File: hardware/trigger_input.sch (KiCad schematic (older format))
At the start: 7 parts

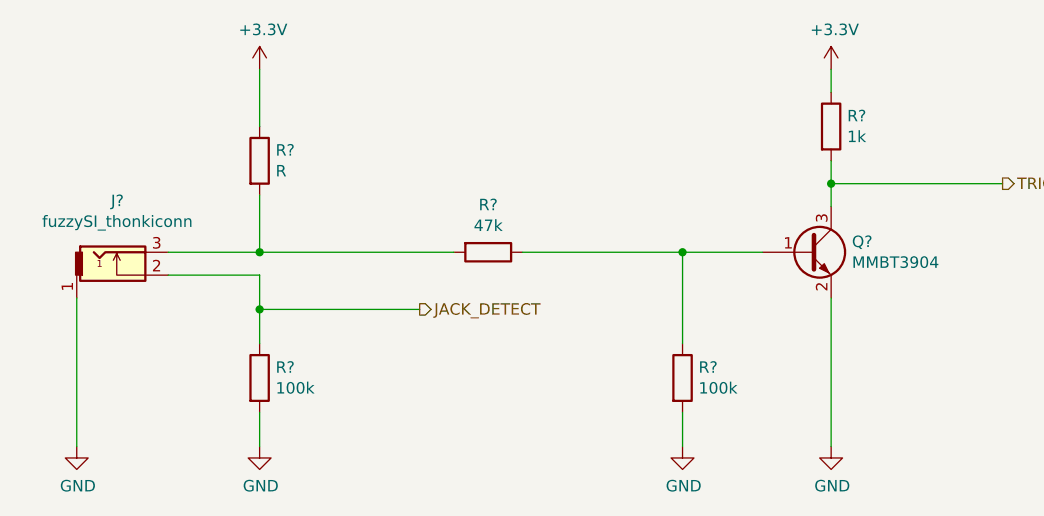
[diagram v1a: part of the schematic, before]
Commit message: Add CV-out schematics
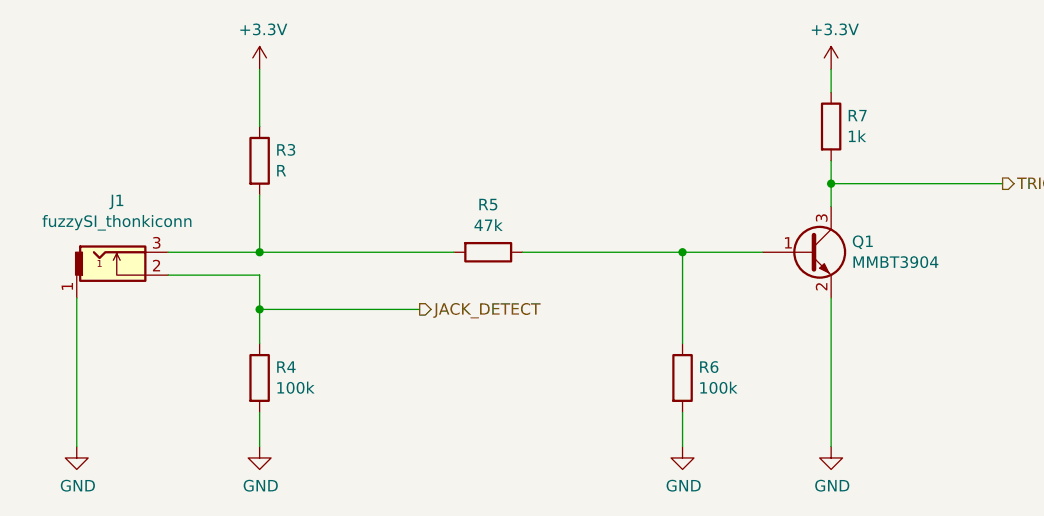
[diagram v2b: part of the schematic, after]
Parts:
- gave numbers to parts that had none: 7
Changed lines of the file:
@@
 $Descr A4 11693 8268
 encoding utf-8
-Sheet 2 3
+Sheet 2 4
 Title ""
 Date ""
@@
 $EndDescr
 $Comp
-L power:+3.3V #PWR?
+L power:+3.3V #PWR06
 U 1 1 5ED56FD6
 P 4700 2650
-F 0 "#PWR?" H 4700 2500 50  0001 C CNN
+F 0 "#PWR06" H 4700 2500 50  0001 C CNN
 F 1 "+3.3V" H 4715 2823 50  0000 C CNN
 F 2 "" H 4700 2650 50  0001 C CNN
@@
 $EndComp
 $Comp
-L power:GND #PWR?
+L power:GND #PWR07
 U 1 1 5ED578BC
 P 4700 4300
-F 0 "#PWR?" H 4700 4050 50  0001 C CNN
+F 0 "#PWR07" H 4700 4050 50  0001 C CNN
 F 1 "GND" H 4705 4127 50  0000 C CNN
 F 2 "" H 4700 4300 50  0001 C CNN
@@
 $EndComp
 $Comp
-L Transistor_BJT:MMBT3904 Q?
+L Transistor_BJT:MMBT3904 Q1
 U 1 1 5ED5AD18
 P 7100 3450
-F 0 "Q?" H 7291 3496 50  0000 L CNN
+F 0 "Q1" H 7291 3496 50  0000 L CNN
 F 1 "MMBT3904" H 7291 3405 50  0000 L CNN
 F 2 "Package_TO_SOT_SMD:SOT-23" H 7300 3375 50  0001 L CIN
@@
 $EndComp
 $Comp
-L Device:R R?
+L Device:R R3
 U 1 1 5ED61718
 P 4700 3050
-F 0 "R?" H 4770 3096 50  0000 L CNN
+F 0 "R3" H 4770 3096 50  0000 L CNN
 F 1 "R" H 4770 3005 50  0000 L CNN
 F 2 "" V 4630 3050 50  0001 C CNN
@@
 $EndComp
 $Comp
-L Device:R R?
+L Device:R R7
 U 1 1 5ED61C77
 P 7200 2900
-F 0 "R?" H 7270 2946 50  0000 L CNN
+F 0 "R7" H 7270 2946 50  0000 L CNN
 F 1 "1k" H 7270 2855 50  0000 L CNN
 F 2 "" V 7130 2900 50  0001 C CNN
@@
 $EndComp
 $Comp
-L Device:R R?
+L Device:R R4
 U 1 1 5ED61E0C
 P 4700 4000
-F 0 "R?" H 4770 4046 50  0000 L CNN
+F 0 "R4" H 4770 4046 50  0000 L CNN
 F 1 "100k" H 4770 3955 50  0000 L CNN
 F 2 "" V 4630 4000 50  0001 C CNN
@@
 $EndComp
 $Comp
-L Device:R R?
+L Device:R R5
 U 1 1 5ED62145
 P 5700 3450
-F 0 "R?" V 5493 3450 50  0000 C CNN
+F 0 "R5" V 5493 3450 50  0000 C CNN
 F 1 "47k" V 5584 3450 50  0000 C CNN
 F 2 "" V 5630 3450 50  0001 C CNN
@@
 $EndComp
 $Comp
-L Device:R R?
+L Device:R R6
 U 1 1 5ED6232E
 P 6550 4000
-F 0 "R?" H 6620 4046 50  0000 L CNN
+F 0 "R6" H 6620 4046 50  0000 L CNN
 F 1 "100k" H 6620 3955 50  0000 L CNN
 F 2 "" V 6480 4000 50  0001 C CNN
@@
 	4700 2650 4700 2900
 $Comp
-L power:+3.3V #PWR?
+L power:+3.3V #PWR09
 U 1 1 5ED6C9CF
 P 7200 2650
-F 0 "#PWR?" H 7200 2500 50  0001 C CNN
+F 0 "#PWR09" H 7200 2500 50  0001 C CNN
 F 1 "+3.3V" H 7215 2823 50  0000 C CNN
 F 2 "" H 7200 2650 50  0001 C CNN
@@
 Connection ~ 6550 3450
 $Comp
-L power:GND #PWR?
+L power:GND #PWR08
 U 1 1 5ED7253E
 P 6550 4300
-F 0 "#PWR?" H 6550 4050 50  0001 C CNN
+F 0 "#PWR08" H 6550 4050 50  0001 C CNN
 F 1 "GND" H 6555 4127 50  0000 C CNN
 F 2 "" H 6550 4300 50  0001 C CNN
@@
 	6550 4300 6550 4150
 $Comp
-L power:GND #PWR?
+L power:GND #PWR010
 U 1 1 5ED73092
 P 7200 4300
-F 0 "#PWR?" H 7200 4050 50  0001 C CNN
+F 0 "#PWR010" H 7200 4050 50  0001 C CNN
 F 1 "GND" H 7205 4127 50  0000 C CNN
 F 2 "" H 7200 4300 50  0001 C CNN
@@
 	3900 3650 3900 4300
 $Comp
-L power:GND #PWR?
+L power:GND #PWR05
 U 1 1 5ED63404
 P 3900 4300
-F 0 "#PWR?" H 3900 4050 50  0001 C CNN
+F 0 "#PWR05" H 3900 4050 50  0001 C CNN
 F 1 "GND" H 3905 4127 50  0000 C CNN
 F 2 "" H 3900 4300 50  0001 C CNN
@@
 $EndComp
 $Comp
-L thonkiconn_jackSocket_fuzzySi:fuzzySI_thonkiconn J?
+L thonkiconn_jackSocket_fuzzySi:fuzzySI_thonkiconn J1
 U 1 1 5ED5F1B0
 P 4100 3550
-F 0 "J?" H 4078 3875 50  0000 C CNN
+F 0 "J1" H 4078 3875 50  0000 C CNN
 F 1 "fuzzySI_thonkiconn" H 4078 3784 50  0000 C CNN
 F 2 "" H 4350 3650 50  0001 C CNN

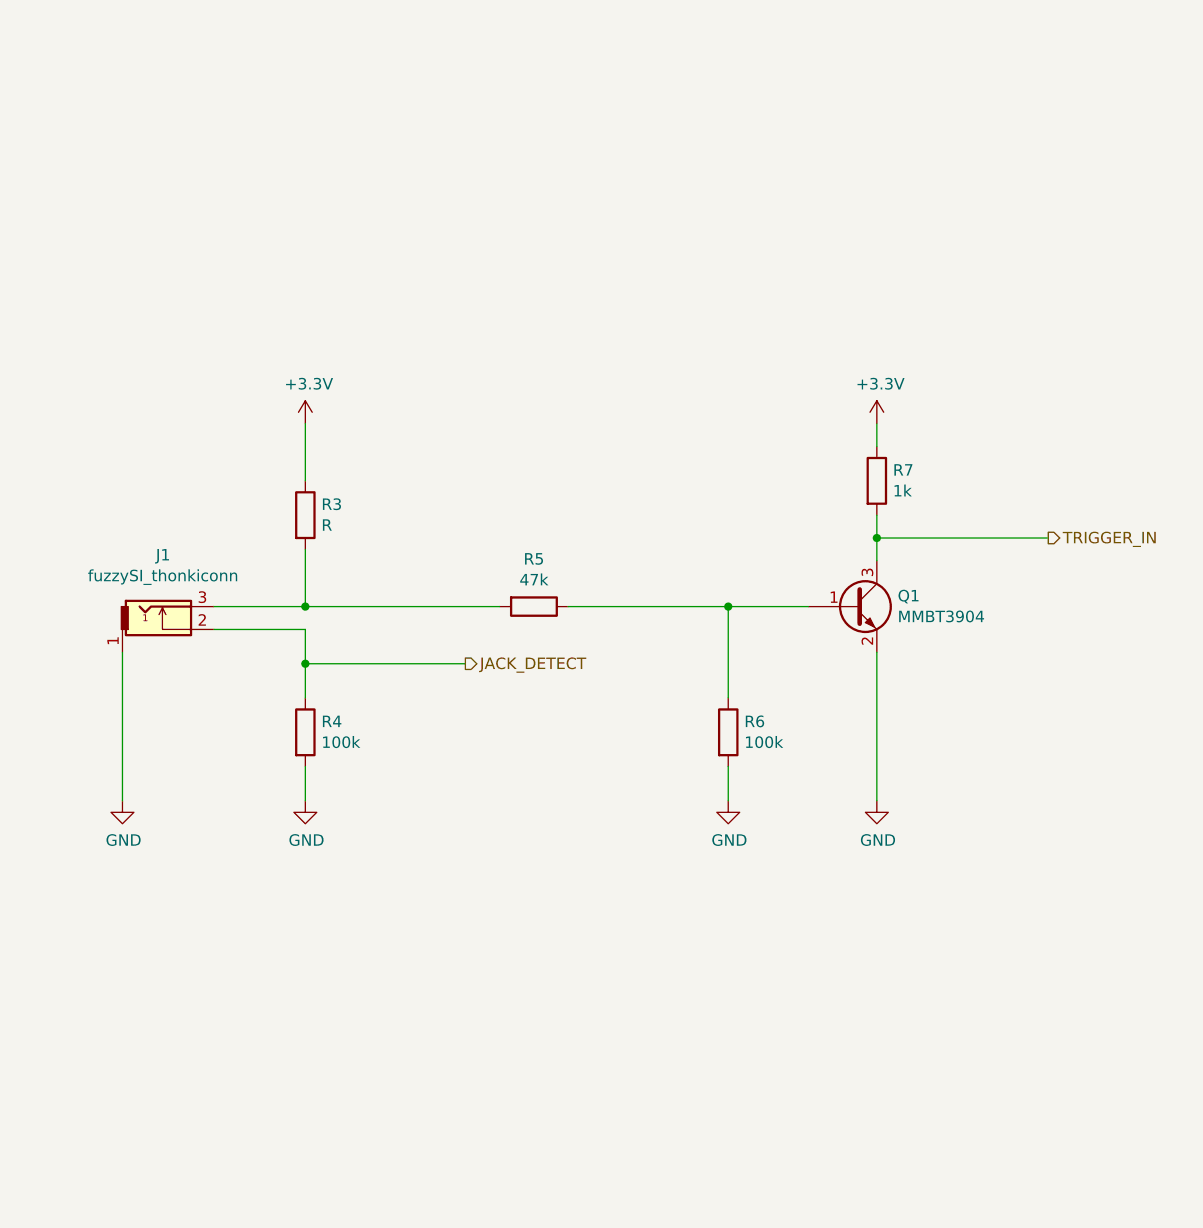
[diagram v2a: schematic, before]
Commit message: Add CV inputs schematics
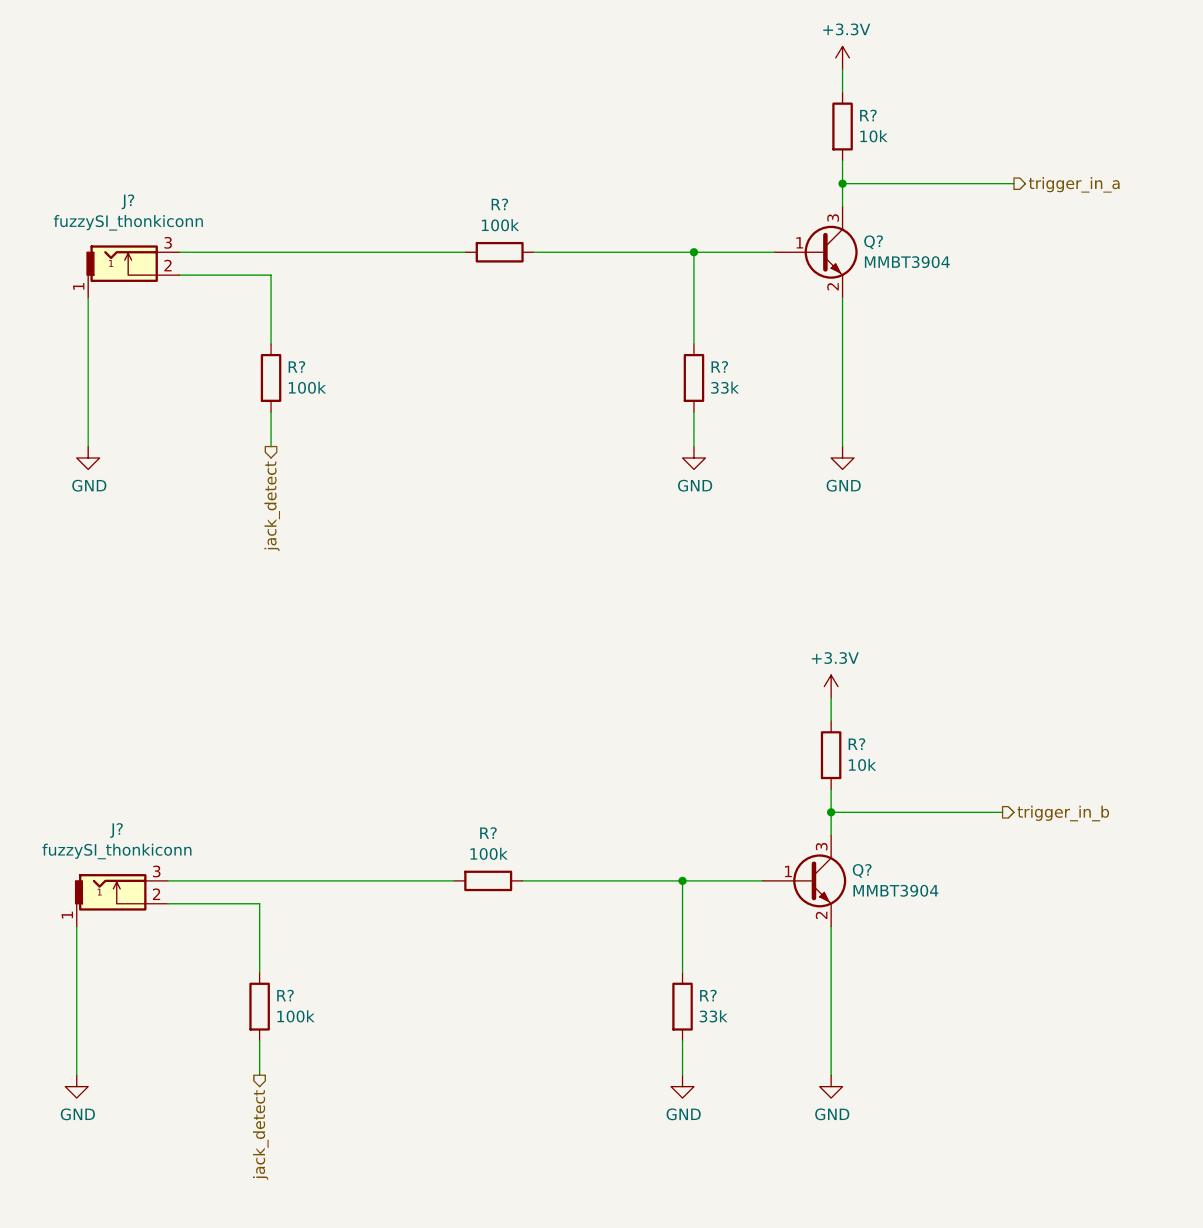
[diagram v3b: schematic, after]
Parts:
- removed R3: R, symbol Device:R
- added J?: fuzzySI_thonkiconn, symbol thonkiconn_jackSocket_fuzzySi:fuzzySI_thonkiconn
- added Q?: MMBT3904, Package_TO_SOT_SMD:SOT-23, symbol Transistor_BJT:MMBT3904
- added R?: 10k, symbol Device:R
- added R? (x2): 100k, symbol Device:R
- added R?: 33k, symbol Device:R
- R?: renamed from R7; value 1k -> 10k
- R?: renamed from R5; value 47k -> 100k
- R?: renamed from R6; value 100k -> 33k
- renumbered J1 to J?, Q1 to Q?, R4 to R?
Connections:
- net +3V3: now also R?.1
- net GND: now also J?.1, Q?.2 (E), R?.2; no longer R?.2
- net JACK_DETECT: no longer names the net of J?.2, R?.1
- net TRIGGER_IN renamed trigger_in_a
- new net: Q?.1 (B), R?.1, R?.1
- new net: J?.2, R?.1
- new net: J?.3, R?.2
- new net jack_detect: R?.2, R?.2
- new net trigger_in_b: Q?.3 (C), R?.2
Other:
- moved on the sheet: J?, Q?, R?

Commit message: Add more schematics:
- Faders
- Step LEDs
- Trigger output
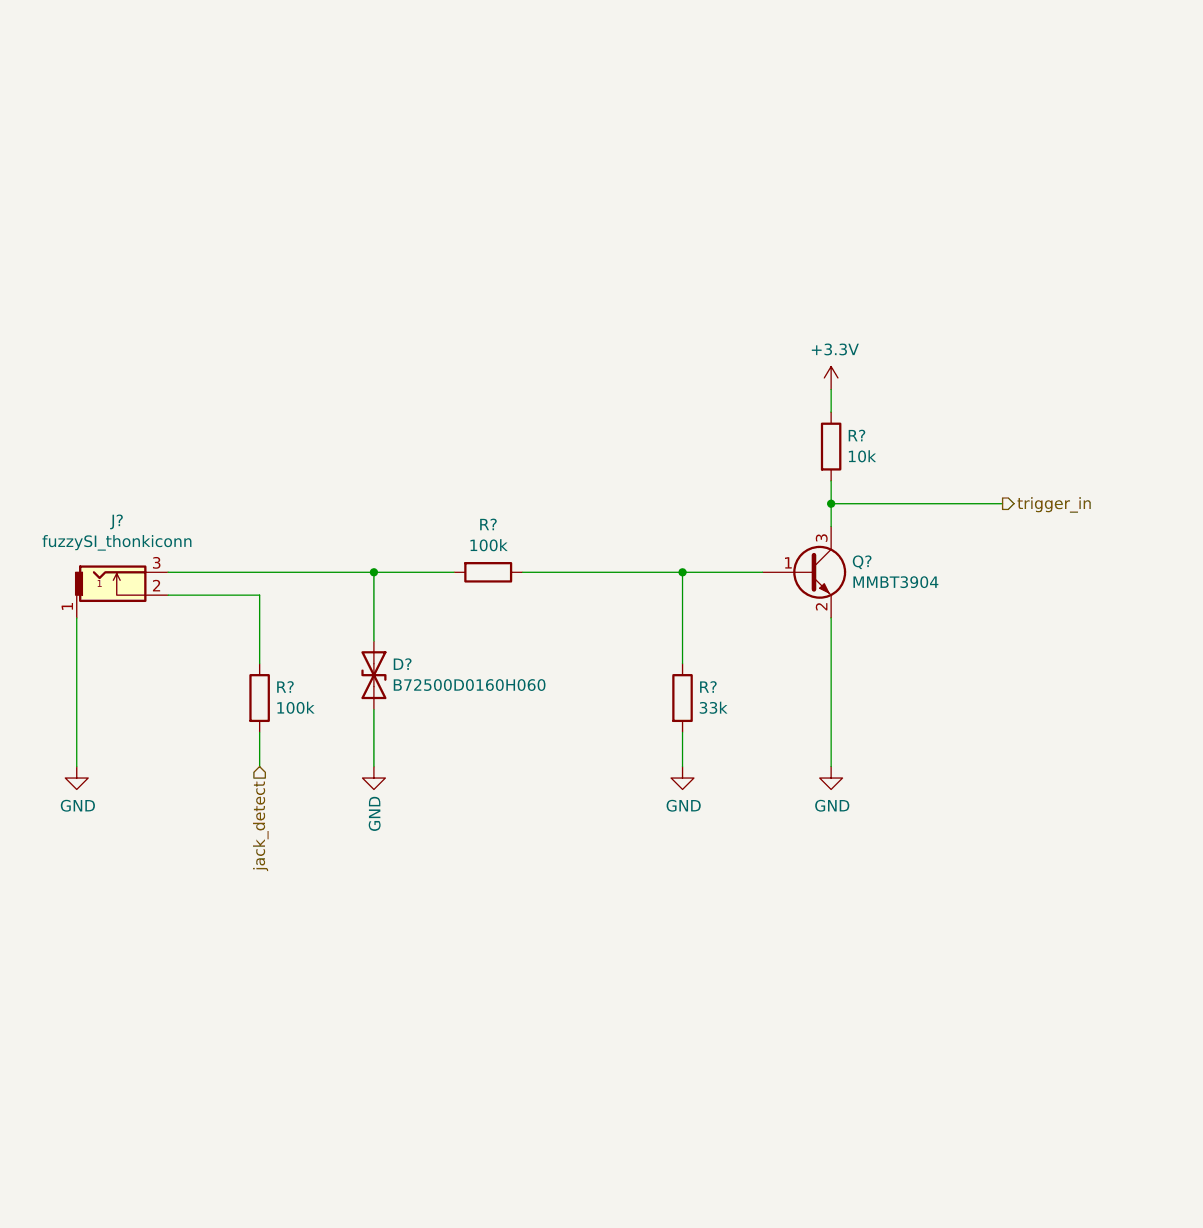
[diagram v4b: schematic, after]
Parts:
- removed J?: fuzzySI_thonkiconn, symbol thonkiconn_jackSocket_fuzzySi:fuzzySI_thonkiconn
- removed Q?: MMBT3904, Package_TO_SOT_SMD:SOT-23, symbol Transistor_BJT:MMBT3904
- removed R?: 10k, symbol Device:R
- removed R? (x2): 100k, symbol Device:R
- removed R?: 33k, symbol Device:R
- added D?: B72500D0160H060, Diode_SMD:D_0603_1608Metric, symbol Device:D_TVS
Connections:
- net GND: now also D?.2 (A2)
- net at J?.3, R?.2: now also D?.1 (A1)
- net trigger_in_a renamed trigger_in
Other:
- moved on the sheet: J?, Q?, R?

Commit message: Minor adjustments to schematics before PCB
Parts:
- removed J?: fuzzySI_thonkiconn, symbol thonkiconn_jackSocket_fuzzySi:fuzzySI_thonkiconn
- added J7: PJ398SM, Connector_Audio:Jack_3.5mm_QingPu_WQP-PJ398SM_Vertical_CircularHoles, symbol Connector:AudioJack2_SwitchT
- R14, R15, R16, R17: renamed from R?; footprint (none) -> Resistor_SMD:R_0603_1608Metric
- gave numbers to parts that had none: 2
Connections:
- net GND: now also J7.S
- net at R14.1: now also J7.TN
- net at D9.1 (A1), R15.2: now also J7.T
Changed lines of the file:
@@
 $Descr A4 11693 8268
 encoding utf-8
-Sheet 2 10
+Sheet 6 11
 Title ""
 Date ""
@@
 $EndDescr
 $Comp
-L Transistor_BJT:MMBT3904 Q?
+L Transistor_BJT:MMBT3904 Q1
 U 1 1 5ED5AD18
 P 6900 3300
-F 0 "Q?" H 7091 3346 50  0000 L CNN
+F 0 "Q1" H 7091 3346 50  0000 L CNN
 F 1 "MMBT3904" H 7091 3255 50  0000 L CNN
 F 2 "Package_TO_SOT_SMD:SOT-23" H 7100 3225 50  0001 L CIN
@@
 $EndComp
 $Comp
-L Device:R R?
+L Device:R R17
 U 1 1 5ED61C77
 P 7000 2750
-F 0 "R?" H 7070 2796 50  0000 L CNN
+F 0 "R17" H 7070 2796 50  0000 L CNN
 F 1 "10k" H 7070 2705 50  0000 L CNN
-F 2 "" V 6930 2750 50  0001 C CNN
+F 2 "Resistor_SMD:R_0603_1608Metric" V 6930 2750 50  0001 C CNN
 F 3 "~" H 7000 2750 50  0001 C CNN
 	1    7000 2750
@@
 $EndComp
 $Comp
-L Device:R R?
+L Device:R R14
 U 1 1 5ED61E0C
 P 4500 3850
-F 0 "R?" H 4570 3896 50  0000 L CNN
+F 0 "R14" H 4570 3896 50  0000 L CNN
 F 1 "100k" H 4570 3805 50  0000 L CNN
-F 2 "" V 4430 3850 50  0001 C CNN
+F 2 "Resistor_SMD:R_0603_1608Metric" V 4430 3850 50  0001 C CNN
 F 3 "~" H 4500 3850 50  0001 C CNN
 	1    4500 3850
@@
 $EndComp
 $Comp
-L Device:R R?
+L Device:R R15
 U 1 1 5ED62145
 P 5500 3300
-F 0 "R?" V 5293 3300 50  0000 C CNN
+F 0 "R15" V 5293 3300 50  0000 C CNN
 F 1 "100k" V 5384 3300 50  0000 C CNN
-F 2 "" V 5430 3300 50  0001 C CNN
+F 2 "Resistor_SMD:R_0603_1608Metric" V 5430 3300 50  0001 C CNN
 F 3 "~" H 5500 3300 50  0001 C CNN
 	1    5500 3300
@@
 $EndComp
 $Comp
-L Device:R R?
+L Device:R R16
 U 1 1 5ED6232E
 P 6350 3850
-F 0 "R?" H 6420 3896 50  0000 L CNN
+F 0 "R16" H 6420 3896 50  0000 L CNN
 F 1 "33k" H 6420 3805 50  0000 L CNN
-F 2 "" V 6280 3850 50  0001 C CNN
+F 2 "Resistor_SMD:R_0603_1608Metric" V 6280 3850 50  0001 C CNN
 F 3 "~" H 6350 3850 50  0001 C CNN
 	1    6350 3850
@@
 	4500 4000 4500 4150
 $Comp
-L power:+3.3V #PWR0101
+L power:+3.3V #PWR046
 U 1 1 5ED6C9CF
 P 7000 2500
-F 0 "#PWR0101" H 7000 2350 50  0001 C CNN
+F 0 "#PWR046" H 7000 2350 50  0001 C CNN
 F 1 "+3.3V" H 7015 2673 50  0000 C CNN
 F 2 "" H 7000 2500 50  0001 C CNN
@@
 Connection ~ 6350 3300
 $Comp
-L power:GND #PWR0102
+L power:GND #PWR045
 U 1 1 5ED7253E
 P 6350 4150
-F 0 "#PWR0102" H 6350 3900 50  0001 C CNN
+F 0 "#PWR045" H 6350 3900 50  0001 C CNN
 F 1 "GND" H 6355 3977 50  0000 C CNN
 F 2 "" H 6350 4150 50  0001 C CNN
@@
 	6350 4150 6350 4000
 $Comp
-L power:GND #PWR0103
+L power:GND #PWR047
 U 1 1 5ED73092
 P 7000 4150
-F 0 "#PWR0103" H 7000 3900 50  0001 C CNN
+F 0 "#PWR047" H 7000 3900 50  0001 C CNN
 F 1 "GND" H 7005 3977 50  0000 C CNN
 F 2 "" H 7000 4150 50  0001 C CNN
@@
 Wire Wire Line
 	4100 3400 4500 3400
-Wire Wire Line
-	3700 3500 3700 4150
 $Comp
-L power:GND #PWR0104
+L power:GND #PWR043
 U 1 1 5ED63404
-P 3700 4150
-F 0 "#PWR0104" H 3700 3900 50  0001 C CNN
-F 1 "GND" H 3705 3977 50  0000 C CNN
-F 2 "" H 3700 4150 50  0001 C CNN
-F 3 "" H 3700 4150 50  0001 C CNN
-	1    3700 4150
-	1    0    0    -1
-$EndComp
-$Comp
-L thonkiconn_jackSocket_fuzzySi:fuzzySI_thonkiconn J?
-U 1 1 5ED5F1B0
-P 3900 3400
-F 0 "J?" H 3878 3725 50  0000 C CNN
-F 1 "fuzzySI_thonkiconn" H 3878 3634 50  0000 C CNN
-F 2 "" H 4150 3500 50  0001 C CNN
-F 3 "" H 4150 3500 50  0001 C CNN
-	1    3900 3400
-	1    0    0    -1
+P 4450 3000
+F 0 "#PWR043" H 4450 2750 50  0001 C CNN
+F 1 "GND" H 4455 2827 50  0000 C CNN
+F 2 "" H 4450 3000 50  0001 C CNN
+F 3 "" H 4450 3000 50  0001 C CNN
+	1    4450 3000
+	-1   0    0    1
 $EndComp
 Wire Wire Line
@@
 P 5000 3750
 AR Path="/5FCA3E21/5FDB7947" Ref="D?"  Part="1"
-AR Path="/5ED4085B/5FDB7947" Ref="D?"  Part="1"
-F 0 "D?" V 4954 3830 50  0000 L CNN
+AR Path="/5ED4085B/5FDB7947" Ref="D9"  Part="1"
+F 0 "D9" V 4954 3830 50  0000 L CNN
 F 1 "B72500D0160H060" V 5045 3830 50  0000 L CNN
 F 2 "Diode_SMD:D_0603_1608Metric" H 5000 3750 50  0001 C CNN
@@
 AR Path="/5ED37B53/5FB5AC07/5FDB794E" Ref="#PWR?"  Part="1"
 AR Path="/5FCA3E21/5FDB794E" Ref="#PWR?"  Part="1"
-AR Path="/5ED4085B/5FDB794E" Ref="#PWR0105"  Part="1"
-F 0 "#PWR0105" H 5000 3900 50  0001 C CNN
+AR Path="/5ED4085B/5FDB794E" Ref="#PWR044"  Part="1"
+F 0 "#PWR044" H 5000 3900 50  0001 C CNN
 F 1 "GND" V 5005 4022 50  0000 R CNN
 F 2 "" H 5000 4150 50  0001 C CNN
@@
 Text HLabel 4500 4150 3    50   Input ~ 0
 jack_detect
+$Comp
+L Connector:AudioJack2_SwitchT J7
+U 1 1 5FEDA01C
+P 3900 3300
+F 0 "J7" H 3932 3625 50  0000 C CNN
+F 1 "PJ398SM" H 3932 3534 50  0000 C CNN
+F 2 "Connector_Audio:Jack_3.5mm_QingPu_WQP-PJ398SM_Vertical_CircularHoles" H 3900 3300 50  0001 C CNN
+F 3 "~" H 3900 3300 50  0001 C CNN
+	1    3900 3300
+	1    0    0    -1
+$EndComp
+Wire Wire Line
+	4100 3200 4450 3200
+Wire Wire Line
+	4450 3200 4450 3000
 $EndSCHEMATC
